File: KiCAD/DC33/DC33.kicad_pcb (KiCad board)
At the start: 4 copper layers, 198.5 x 104.3 mm, 200 parts, among them J1 SAO, J2 PPTC201LFBN-RC, J3 PPTC201LFBN-RC, J4 282834-3, J5 282834-3, J6 FPC-30, J7 S2B-PH-K-S(LF)(SN), Q1 FDN359BN, Q2 CSD17576Q5B, Q3 CSD17576Q5B, U1 PICO2, U10 PCA9536DRG4, U11 ADG849YKSZ-REEL, U12 ADG849YKSZ-REEL, U13 MCP2558FD-H_SN, U14 ADG849YKSZ-REEL, U15 ADG849YKSZ-REEL, U16 ADG849YKSZ-REEL, U17 ADG849YKSZ-REEL, U18 ADG849YKSZ-REEL, U19 ADG849YKSZ-REEL, U2 TS5A3359DCUR, U20 MAX33046EASA+T, U21 ALM2403QPWPRQ1, U22 TMUX1108PWR, U23 TL431AIDBZR, U24 TMUX1108PWR, U25 TL431AIDBZR, U26 TL431AIDBZR, U27 TPS22810TDBVRQ1, U28 TL431AIDBZR, U29 TCAL9539PWR, U3 TPSM828303ARDSR, U30 TPS22810TDBVRQ1, U31 MCP2518FD, U4 ADR510ARTZ-REEL7, U5 MC3479, U6 LM4040D20IDBZR, U7 ISL21010CFH315Z-T7A, U8 BQ297xy, U9 BQ25895RTW, Y1 20MHz 18pF

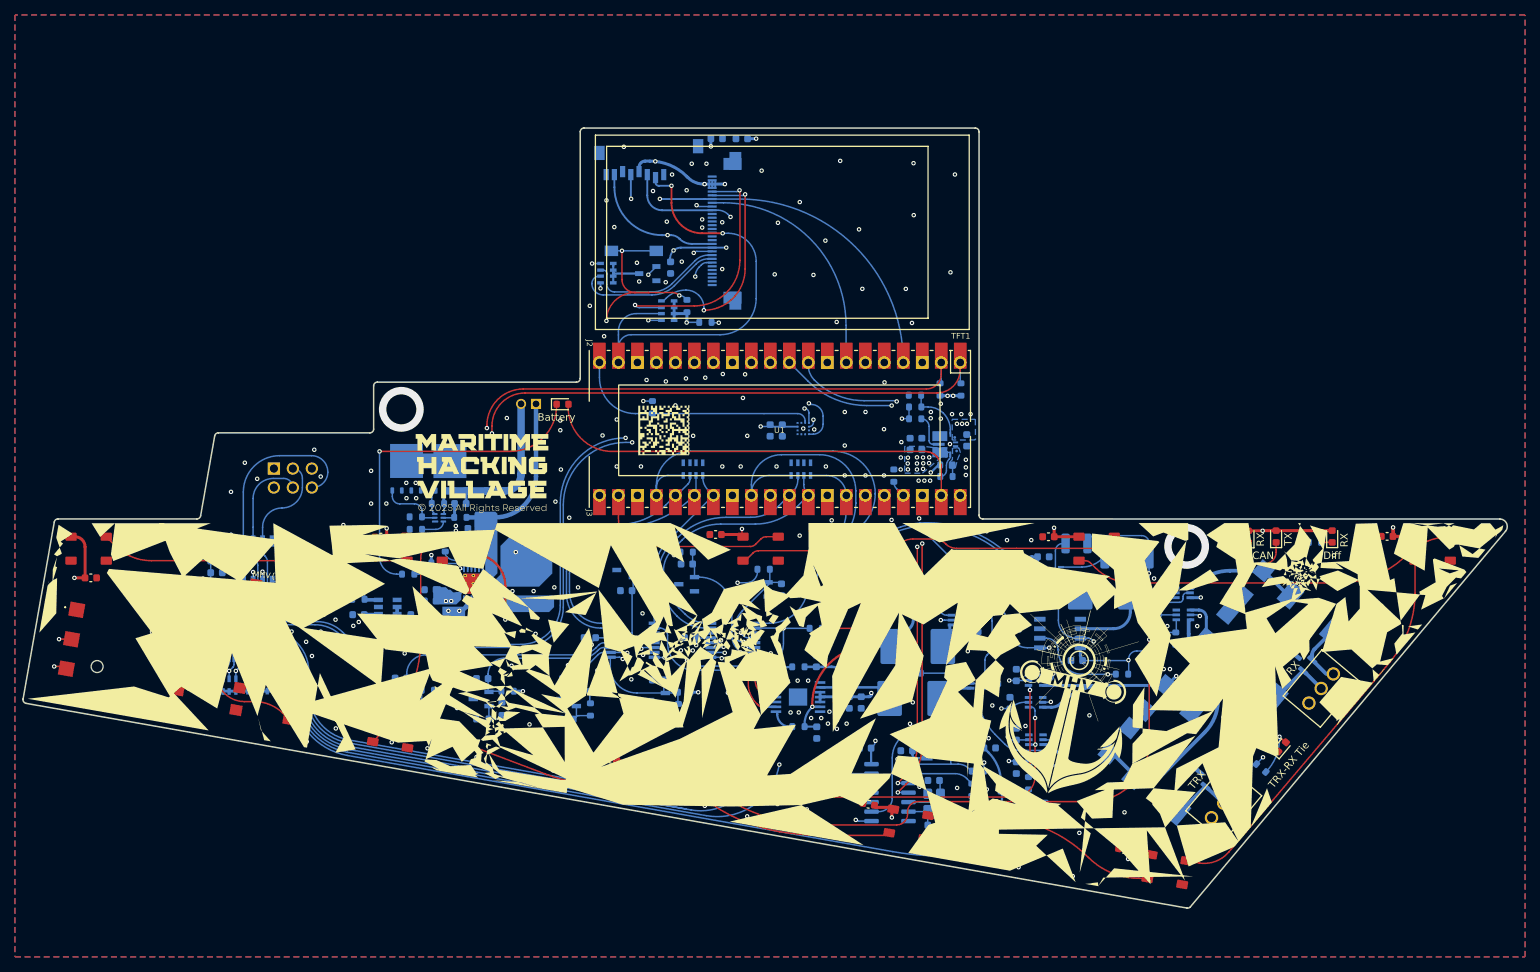
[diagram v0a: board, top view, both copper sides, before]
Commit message: Converted to KiCAD 10.0.4 and removed silkscreen art
Removed some art, refilled the fill zones, appears to be loading better now.
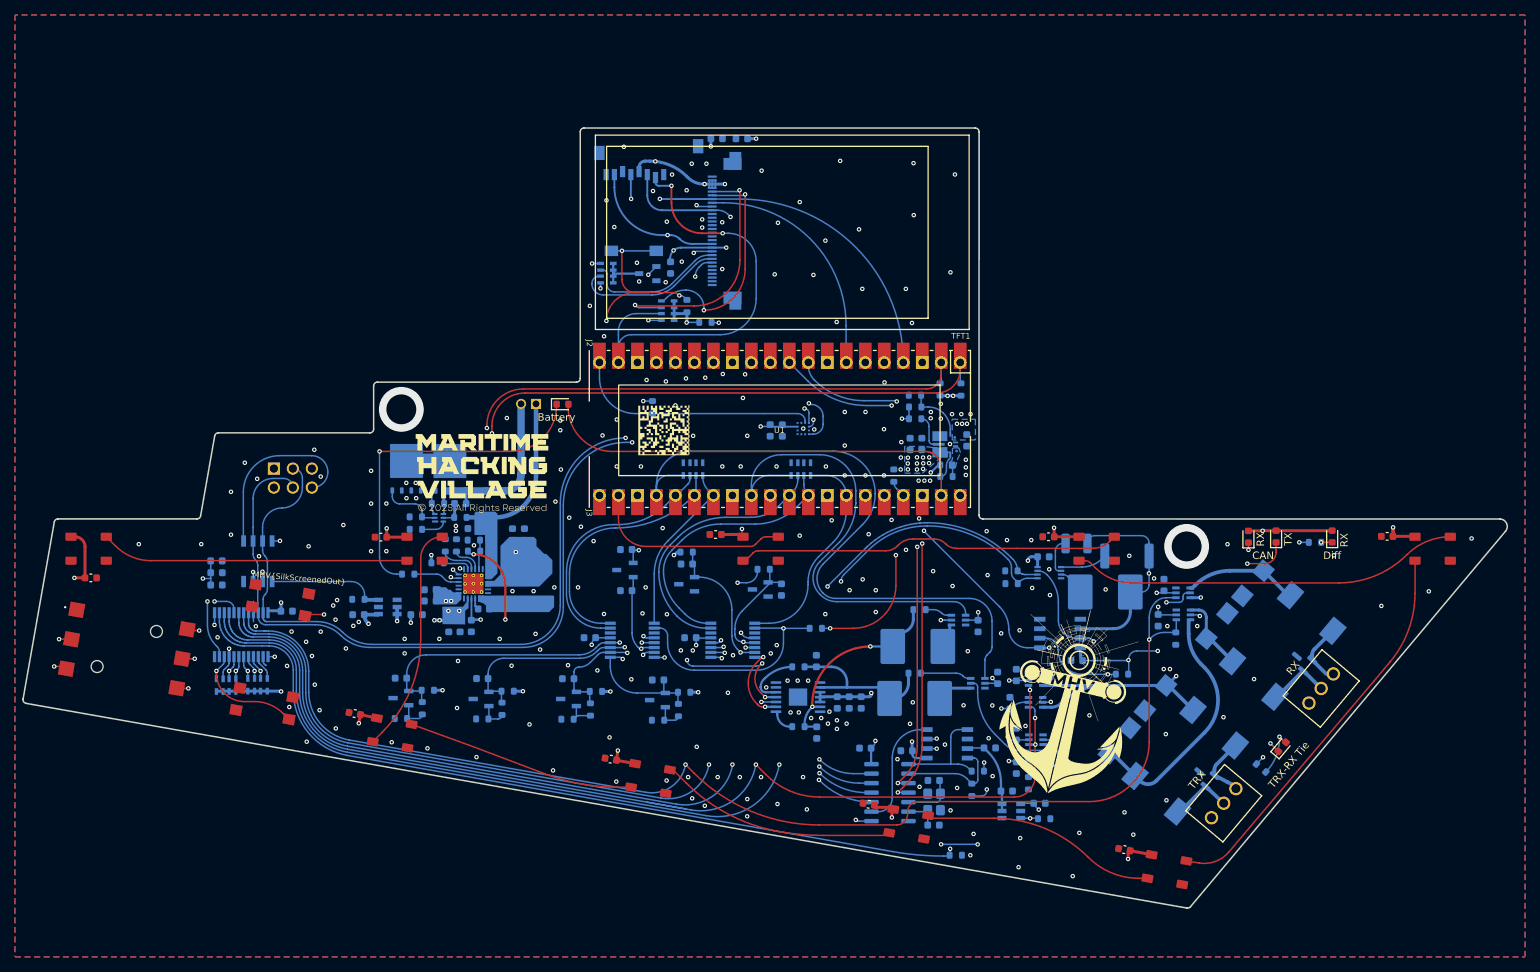
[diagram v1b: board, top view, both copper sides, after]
